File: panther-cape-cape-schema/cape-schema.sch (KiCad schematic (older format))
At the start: 28 parts, among them P1 OUT2 P4, P10 Y_SENSORS, P11 SENSORS+, P12 SENSORS-, P13 SPINCLE_FEEDBACK, P14 SPINDLE, P15 Z_SENSORS, P16 DRIVER_ENABLE_SWITCH, P17 DRIVER_X, P18 DRIVER_Y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

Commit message: added ppp-pahtner-cape's cape schema
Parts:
- P15: footprint Pin_Headers:Pin_Header_Straight_1x02_Pitch2.54mm_SMD_Pin1Left -> Pin_Headers:Pin_Header_Straight_2x01_Pitch2.54mm_SMD
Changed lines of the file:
@@
 F 0 "P15" H 8050 1550 50  0000 C CNN
 F 1 "Z_SENSORS" V 8150 1400 50  0000 C CNN
-F 2 "Pin_Headers:Pin_Header_Straight_1x02_Pitch2.54mm_SMD_Pin1Left" H 8050 1400 50  0001 C CNN
+F 2 "Pin_Headers:Pin_Header_Straight_2x01_Pitch2.54mm_SMD" H 8050 1400 50  0001 C CNN
 F 3 "" H 8050 1400 50  0000 C CNN
 	1    8050 1400

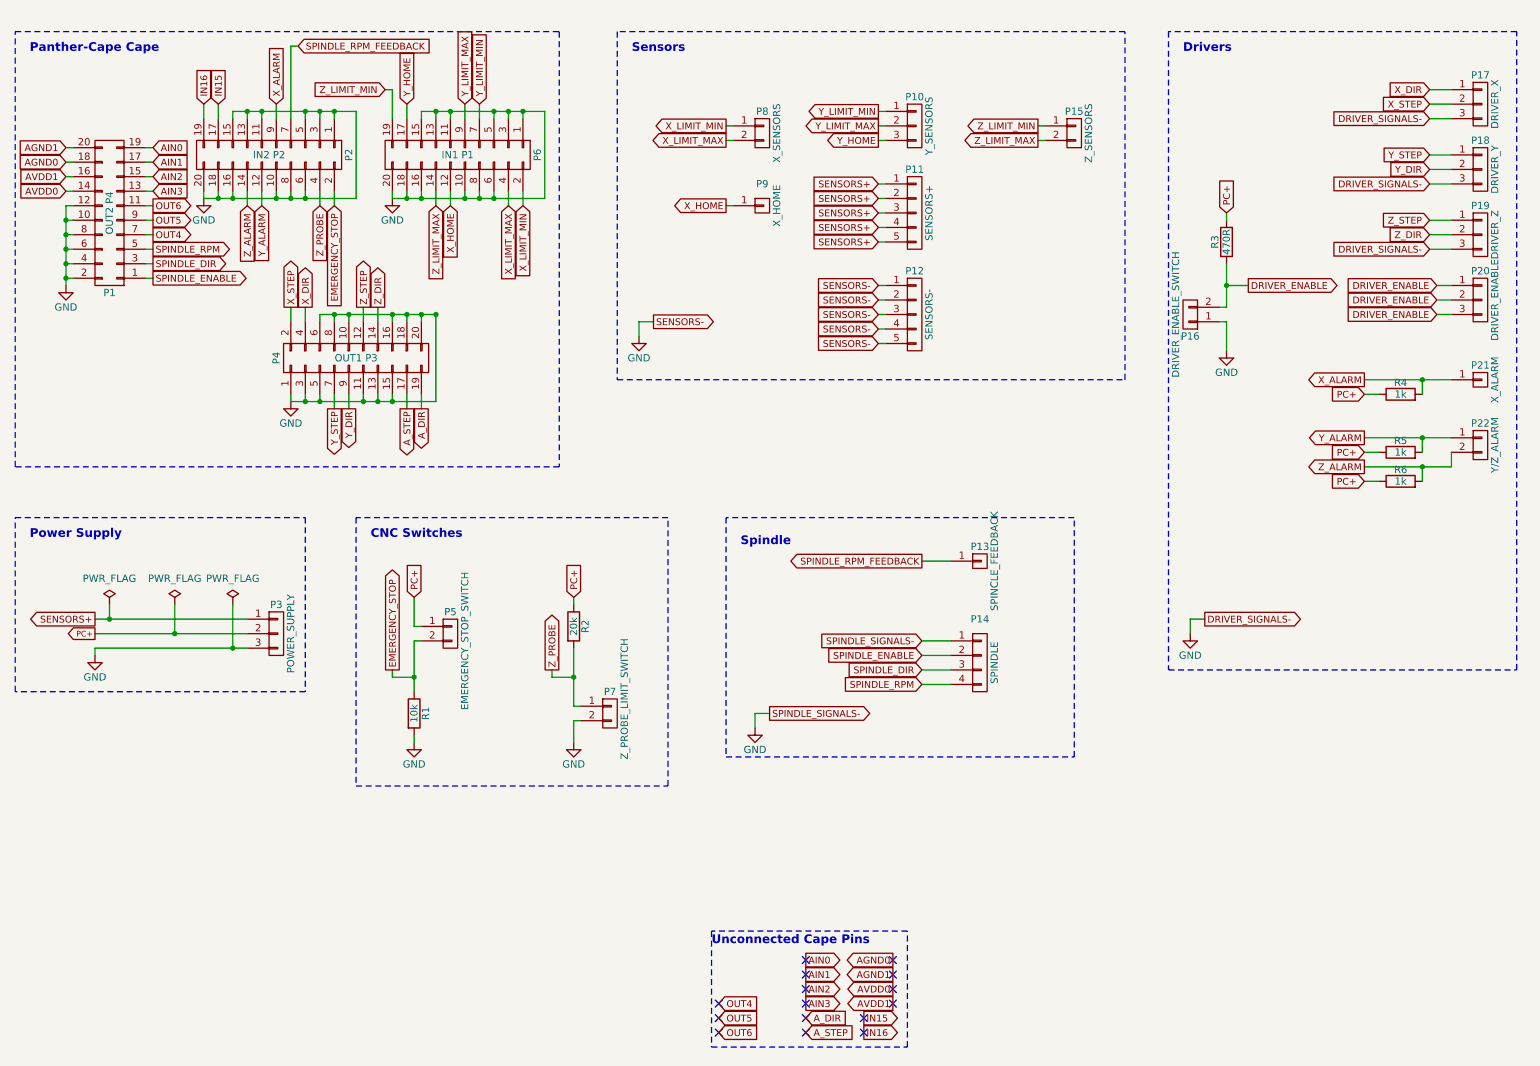
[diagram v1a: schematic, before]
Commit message: routed single layer pcb
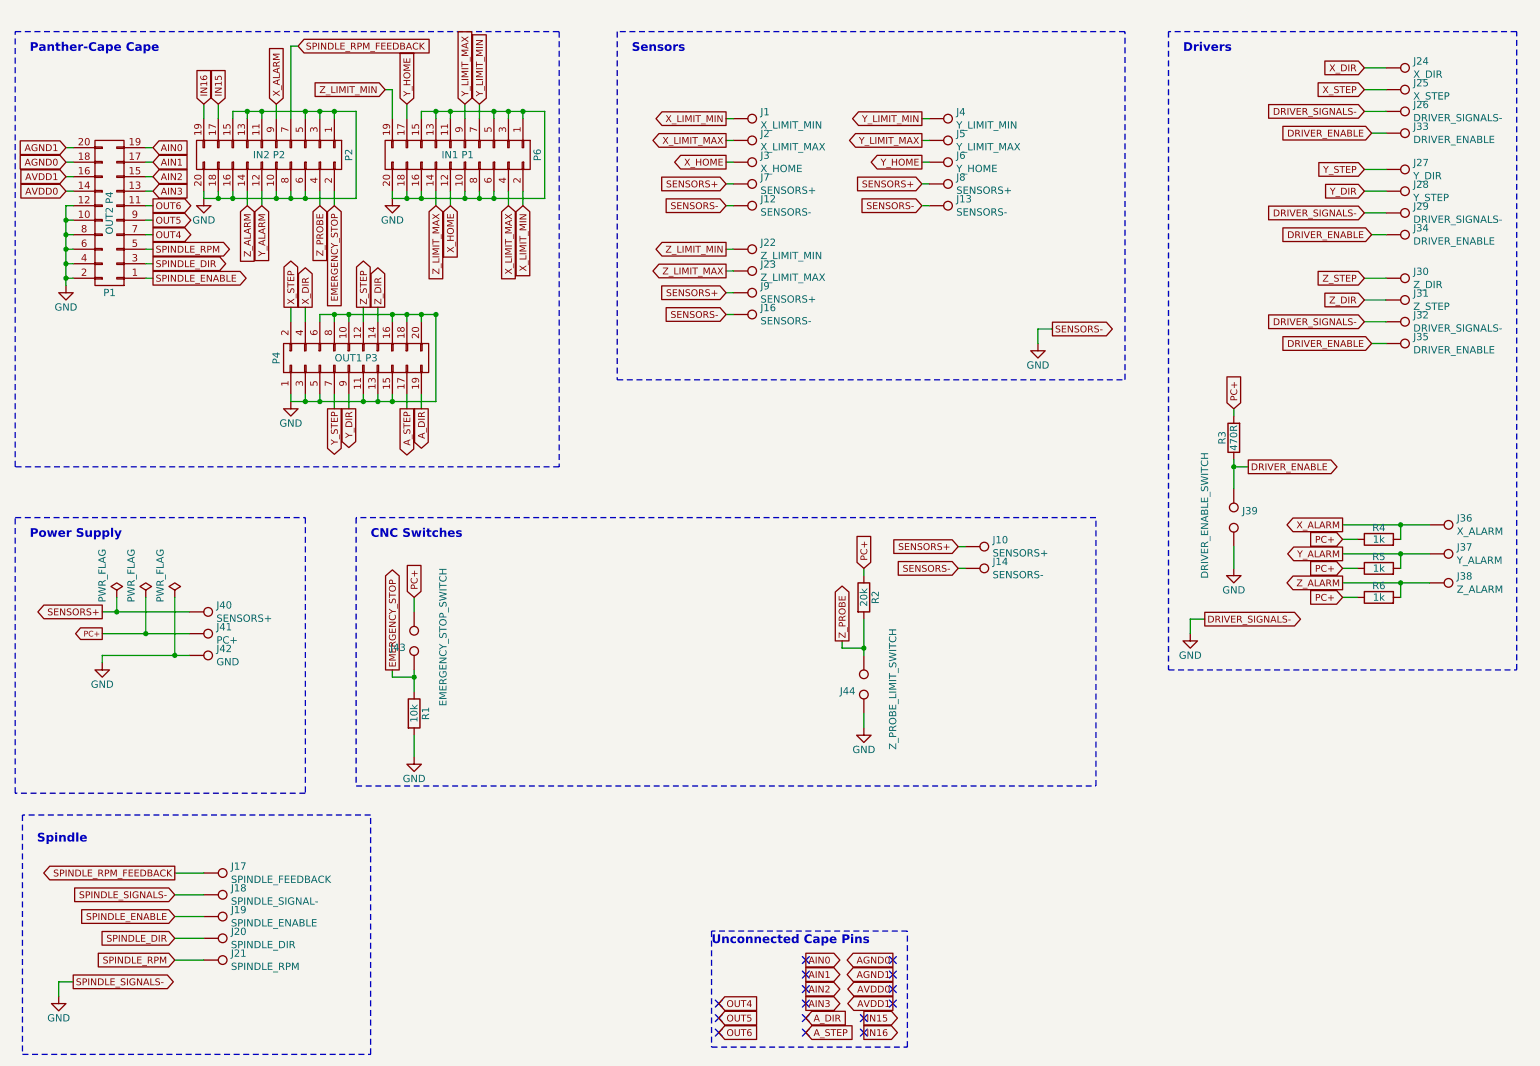
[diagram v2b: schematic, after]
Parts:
- removed P10: Y_SENSORS, Pin_Headers:Pin_Header_Straight_1x03_Pitch2.54mm_SMD_Pin1Left, symbol CONN_01X03
- removed P11: SENSORS+, Pin_Headers:Pin_Header_Straight_1x05_Pitch2.54mm_SMD_Pin1Left, symbol CONN_01X05
- removed P12: SENSORS-, Pin_Headers:Pin_Header_Straight_1x05_Pitch2.54mm_SMD_Pin1Left, symbol CONN_01X05
- removed P13: SPINCLE_FEEDBACK, Pin_Headers:Pin_Header_Straight_1x01_Pitch2.54mm, symbol CONN_01X01
- removed P14: SPINDLE, Pin_Headers:Pin_Header_Straight_1x04_Pitch2.54mm_SMD_Pin1Left, symbol CONN_01X04
- removed P15: Z_SENSORS, Pin_Headers:Pin_Header_Straight_2x01_Pitch2.54mm_SMD, symbol CONN_01X02
- removed P16: DRIVER_ENABLE_SWITCH, Pin_Headers:Pin_Header_Straight_2x01_Pitch2.54mm_SMD, symbol CONN_01X02
- removed P17: DRIVER_X, Pin_Headers:Pin_Header_Straight_1x03_Pitch2.54mm_SMD_Pin1Left, symbol CONN_01X03
- removed P18: DRIVER_Y, Pin_Headers:Pin_Header_Straight_1x03_Pitch2.54mm_SMD_Pin1Left, symbol CONN_01X03
- removed P19: DRIVER_Z, Pin_Headers:Pin_Header_Straight_1x03_Pitch2.54mm_SMD_Pin1Left, symbol CONN_01X03
- removed P20: DRIVER_ENABLE, Pin_Headers:Pin_Header_Straight_1x03_Pitch2.54mm_SMD_Pin1Left, symbol CONN_01X03
- removed P21: X_ALARM, Pin_Headers:Pin_Header_Straight_1x01_Pitch2.54mm, symbol CONN_01X01
- removed P22: Y/Z_ALARM, Pin_Headers:Pin_Header_Straight_1x02_Pitch2.54mm_SMD_Pin1Left, symbol CONN_01X02
- removed P3: POWER_SUPPLY, Pin_Headers:Pin_Header_Straight_1x03_Pitch2.54mm_SMD_Pin1Left, symbol CONN_01X03
- removed P5: EMERGENCY_STOP_SWITCH, Pin_Headers:Pin_Header_Straight_2x01_Pitch2.54mm_SMD, symbol CONN_01X02
- removed P7: Z_PROBE_LIMIT_SWITCH, Pin_Headers:Pin_Header_Straight_2x01_Pitch2.54mm_SMD, symbol CONN_01X02
- removed P8: X_SENSORS, Pin_Headers:Pin_Header_Straight_1x02_Pitch2.54mm_SMD_Pin1Left, symbol CONN_01X02
- removed P9: X_HOME, Pin_Headers:Pin_Header_Straight_1x01_Pitch2.54mm, symbol CONN_01X01
- added J1: X_LIMIT_MIN, Measurement_Points:Test_Point_Keystone_5019_Minature, symbol TEST_1P
- added J10, J40, J7, J8, J9: SENSORS+, Measurement_Points:Test_Point_Keystone_5019_Minature, symbol TEST_1P
- added J12, J13, J14, J16: SENSORS-, Measurement_Points:Test_Point_Keystone_5019_Minature, symbol TEST_1P
- added J17: SPINDLE_FEEDBACK, Measurement_Points:Test_Point_Keystone_5019_Minature, symbol TEST_1P
- added J18: SPINDLE_SIGNAL-, Measurement_Points:Test_Point_Keystone_5019_Minature, symbol TEST_1P
- added J19: SPINDLE_ENABLE, Measurement_Points:Test_Point_Keystone_5019_Minature, symbol TEST_1P
- added J2: X_LIMIT_MAX, Measurement_Points:Test_Point_Keystone_5019_Minature, symbol TEST_1P
- added J20: SPINDLE_DIR, Measurement_Points:Test_Point_Keystone_5019_Minature, symbol TEST_1P
- added J21: SPINDLE_RPM, Measurement_Points:Test_Point_Keystone_5019_Minature, symbol TEST_1P
- added J22: Z_LIMIT_MIN, Measurement_Points:Test_Point_Keystone_5019_Minature, symbol TEST_1P
- added J23: Z_LIMIT_MAX, Measurement_Points:Test_Point_Keystone_5019_Minature, symbol TEST_1P
- added J24: X_DIR, Measurement_Points:Test_Point_Keystone_5019_Minature, symbol TEST_1P
- added J25: X_STEP, Measurement_Points:Test_Point_Keystone_5019_Minature, symbol TEST_1P
- added J26, J29, J32: DRIVER_SIGNALS-, Measurement_Points:Test_Point_Keystone_5019_Minature, symbol TEST_1P
- added J27: Y_DIR, Measurement_Points:Test_Point_Keystone_5019_Minature, symbol TEST_1P
- added J28: Y_STEP, Measurement_Points:Test_Point_Keystone_5019_Minature, symbol TEST_1P
- added J3: X_HOME, Measurement_Points:Test_Point_Keystone_5019_Minature, symbol TEST_1P
- added J30: Z_DIR, Measurement_Points:Test_Point_Keystone_5019_Minature, symbol TEST_1P
- added J31: Z_STEP, Measurement_Points:Test_Point_Keystone_5019_Minature, symbol TEST_1P
- added J33, J34, J35: DRIVER_ENABLE, Measurement_Points:Test_Point_Keystone_5019_Minature, symbol TEST_1P
- added J36: X_ALARM, Measurement_Points:Test_Point_Keystone_5019_Minature, symbol TEST_1P
- added J37: Y_ALARM, Measurement_Points:Test_Point_Keystone_5019_Minature, symbol TEST_1P
- added J38: Z_ALARM, Measurement_Points:Test_Point_Keystone_5019_Minature, symbol TEST_1P
- added J39: DRIVER_ENABLE_SWITCH, Crystals:Crystal_SMD_MicroCrystal_CC1V-T1A-2pin_8.0x3.7mm, symbol TEST_2P
- added J4: Y_LIMIT_MIN, Measurement_Points:Test_Point_Keystone_5019_Minature, symbol TEST_1P
- added J41: PC+, Measurement_Points:Test_Point_Keystone_5019_Minature, symbol TEST_1P
- added J42: GND, Measurement_Points:Test_Point_Keystone_5019_Minature, symbol TEST_1P
- added J43: EMERGENCY_STOP_SWITCH, Crystals:Crystal_SMD_MicroCrystal_CC1V-T1A-2pin_8.0x3.7mm, symbol TEST_2P
- added J44: Z_PROBE_LIMIT_SWITCH, Crystals:Crystal_SMD_MicroCrystal_CC1V-T1A-2pin_8.0x3.7mm, symbol TEST_2P
- added J5: Y_LIMIT_MAX, Measurement_Points:Test_Point_Keystone_5019_Minature, symbol TEST_1P
- added J6: Y_HOME, Measurement_Points:Test_Point_Keystone_5019_Minature, symbol TEST_1P
- P1, P2, P4, P6: footprint Pin_Headers:Pin_Header_Angled_2x10_Pitch2.54mm -> Socket_Strips:Socket_Strip_Straight_2x10
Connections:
- net DRIVER_ENABLE: now also J33.1, J34.1, J35.1, J39.2
- net EMERGENCY_STOP: now also J43.2
- net GND: now also J12.1, J13.1, J14.1, J16.1, J18.1, J26.1, J29.1, J32.1, J39.1, J42.1, J44.2
- net PC+: now also J41.1, J43.1
- net SENSORS+: now also J10.1, J40.1, J7.1, J8.1, J9.1
- net SPINDLE_DIR: now also J20.1
- net SPINDLE_ENABLE: now also J19.1
- net SPINDLE_RPM: now also J21.1
- net SPINDLE_RPM_FEEDBACK: now also J17.1
- net X_ALARM: now also J36.1
- net X_DIR: now also J24.1
- net X_HOME: now also J3.1
- net X_LIMIT_MAX: now also J2.1
- net X_LIMIT_MIN: now also J1.1
- net X_STEP: now also J25.1
- net Y_ALARM: now also J37.1
- net Y_DIR: now also J28.1
- net Y_HOME: now also J6.1
- net Y_LIMIT_MAX: now also J5.1
- net Y_LIMIT_MIN: now also J4.1
- net Y_STEP: now also J27.1
- net Z_ALARM: now also J38.1
- net Z_DIR: now also J31.1
- net Z_LIMIT_MAX: now also J23.1
- net Z_LIMIT_MIN: now also J22.1
- net Z_PROBE: now also J44.1
- net Z_STEP: now also J30.1
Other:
- moved on the sheet: R2, R3, R4, R5, R6

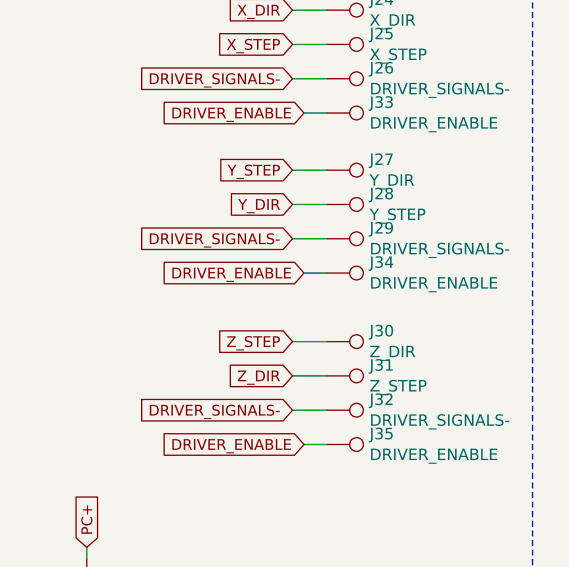
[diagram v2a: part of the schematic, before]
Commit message: fixed connector naming mismatch
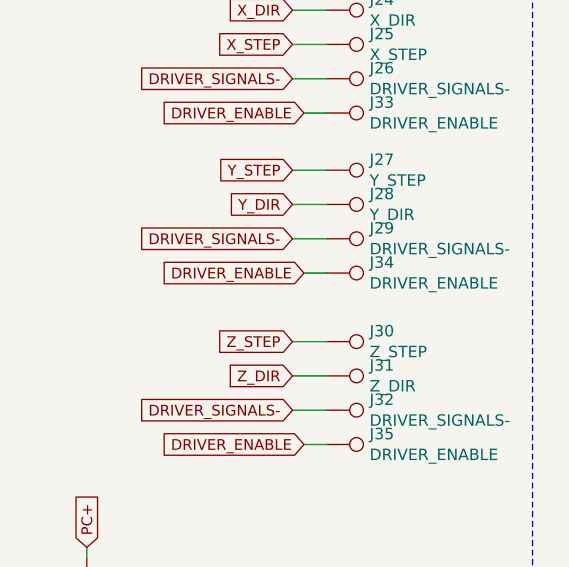
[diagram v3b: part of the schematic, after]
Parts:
- J27: value Y_DIR -> Y_STEP
- J28: value Y_STEP -> Y_DIR
- J30: value Z_DIR -> Z_STEP
- J31: value Z_STEP -> Z_DIR
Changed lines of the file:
@@
 P 10200 1650
 F 0 "J27" V 10154 1837 50  0000 L CNN
-F 1 "Y_DIR" V 10245 1837 50  0000 L CNN
+F 1 "Y_STEP" V 10245 1837 50  0000 L CNN
 F 2 "Measurement_Points:Test_Point_Keystone_5019_Minature" H 2700 -3050 50  0001 C CNN
 F 3 "" H 2700 -3050 50  0001 C CNN
@@
 P 10200 1800
 F 0 "J28" V 10154 1987 50  0000 L CNN
-F 1 "Y_STEP" V 10245 1987 50  0000 L CNN
+F 1 "Y_DIR" V 10245 1987 50  0000 L CNN
 F 2 "Measurement_Points:Test_Point_Keystone_5019_Minature" H 2700 -2900 50  0001 C CNN
 F 3 "" H 2700 -2900 50  0001 C CNN
@@
 P 10200 2400
 F 0 "J30" V 10154 2587 50  0000 L CNN
-F 1 "Z_DIR" V 10245 2587 50  0000 L CNN
+F 1 "Z_STEP" V 10245 2587 50  0000 L CNN
 F 2 "Measurement_Points:Test_Point_Keystone_5019_Minature" H 2700 -2300 50  0001 C CNN
 F 3 "" H 2700 -2300 50  0001 C CNN
@@
 P 10200 2550
 F 0 "J31" V 10154 2737 50  0000 L CNN
-F 1 "Z_STEP" V 10245 2737 50  0000 L CNN
+F 1 "Z_DIR" V 10245 2737 50  0000 L CNN
 F 2 "Measurement_Points:Test_Point_Keystone_5019_Minature" H 2700 -2150 50  0001 C CNN
 F 3 "" H 2700 -2150 50  0001 C CNN
